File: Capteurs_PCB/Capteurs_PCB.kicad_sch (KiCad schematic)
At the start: 22 parts, among them J101 Conn_01x03, J102 Conn_01x02, J103 Conn_02x20_Odd_Even, J104 Conn_ST_STDC14, J3 Prop1, J4 Prop2, J5 Alim_Prop1, J6 Alim_Prop2, J9 LED, SW101 SW_DPDT_x2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

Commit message: Modif PCB
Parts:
- removed C104, C105, C106: 100n, symbol Device:C_Small
- removed J102: Conn_01x02, symbol Connector_Generic:Conn_01x02
- removed J3: Prop1, Connector_PinHeader_2.54mm:PinHeader_1x03_P2.54mm_Vertical, symbol Connector:Conn_01x03_Pin
- removed J4: Prop2, Connector_PinHeader_2.54mm:PinHeader_1x03_P2.54mm_Vertical, symbol Connector:Conn_01x03_Pin
- removed J6: Alim_Prop2, Connector_Hirose:Hirose_DF13-02P-1.25DSA_1x02_P1.25mm_Vertical, symbol Connector:Conn_01x02_Socket
- removed J9: LED, Connector_PinHeader_2.54mm:PinHeader_1x04_P2.54mm_Vertical, symbol Connector:Conn_01x04_Pin
- removed U101: STM32L476RGTx, Package_QFP:LQFP-64_10x10mm_P0.5mm, symbol MCU_ST_STM32L4:STM32L476RGTx
- added J1: Conn_01x04, symbol Connector_Generic:Conn_01x04
- added J2: Conn_01x03, symbol Connector_Generic:Conn_01x03
- added J3: Alim_Prop1, Connector_Hirose:Hirose_DF13-02P-1.25DSA_1x02_P1.25mm_Vertical, symbol Connector:Conn_01x02_Socket
- added U1: STM32L412KBTx, Package_QFP:LQFP-32_7x7mm_P0.8mm, symbol MCU_ST_STM32L4:STM32L412KBTx
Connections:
- net +5V: now also J101.2 (Pin_2), J2.2 (Pin_2), U1.1 (VDD), U1.17 (VDD), U1.5 (VDDA)
- net Earth: no longer J101.1 (Pin_1), J5.2 (Pin_2)
- net FWD1: now also U1.8 (PA2)
- net FWD2: now also U1.18 (PA8)
- net GND: now also J101.1 (Pin_1), J5.1 (Pin_1), J1.1 (Pin_1), J1.3 (Pin_3), J2.1 (Pin_1), J3.1 (Pin_1), U1.16 (VSS), U1.32 (VSS)
- net INT1: now also U1.6 (PA0)
- net INT2: now also U1.7 (PA1)
- net MISO: now also U1.12 (PA6)
- net MOSI: now also U1.13 (PA7)
- net REV1: now also U1.9 (PA3)
- net REV2: now also U1.19 (PA9)
- net SCLK: now also U1.11 (PA5)
- net SS: now also U1.10 (PA4)
- net SigProp1: now also J101.3 (Pin_3), J2.3 (Pin_3), U1.27 (PB4)
- net SigProp2: now also U1.29 (PB6)
- net Sig_LED: now also J1.4 (Pin_4), U1.20 (PA10)
- net UART_RX: now also U1.22 (PA12)
- net UART_TX: now also U1.21 (PA11)
- net VDD_LED: now also J1.2 (Pin_2)
- net V_ALIM_PROP: now also J5.2 (Pin_2), J3.2 (Pin_2); no longer J5.1 (Pin_1)
- no-connect marks 64 -> 38
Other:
- sheet Capteur de Pression ports: added MISO, MOSI, SCLK, SS, VDD; removed none
- sheet Gyroscope-Accéléromètre ports: added CS, IMU_MISO, IMU_MOSI, INT1, INT2, VDD, VDDIO; removed none
- note added: "RaspberryPi"
- note removed: "Branchement RaspberryPi"
- moved on the sheet: C101, C102, C103, C107, H101, H102, H103, H104, J101, J103, J104, J5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

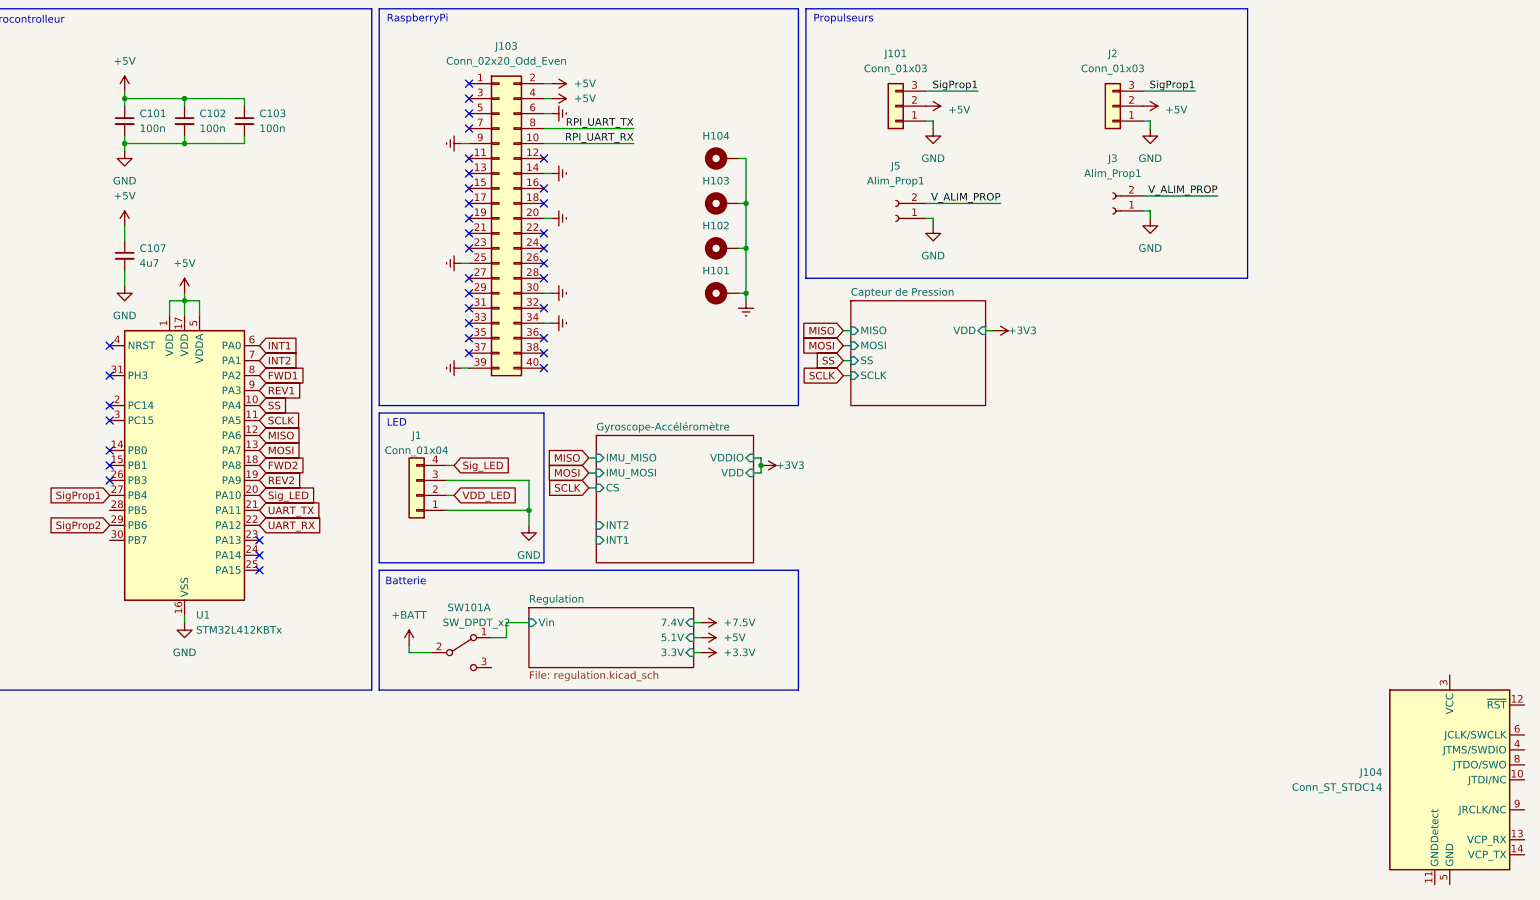
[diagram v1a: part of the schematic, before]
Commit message: kicad changes and starting footprints
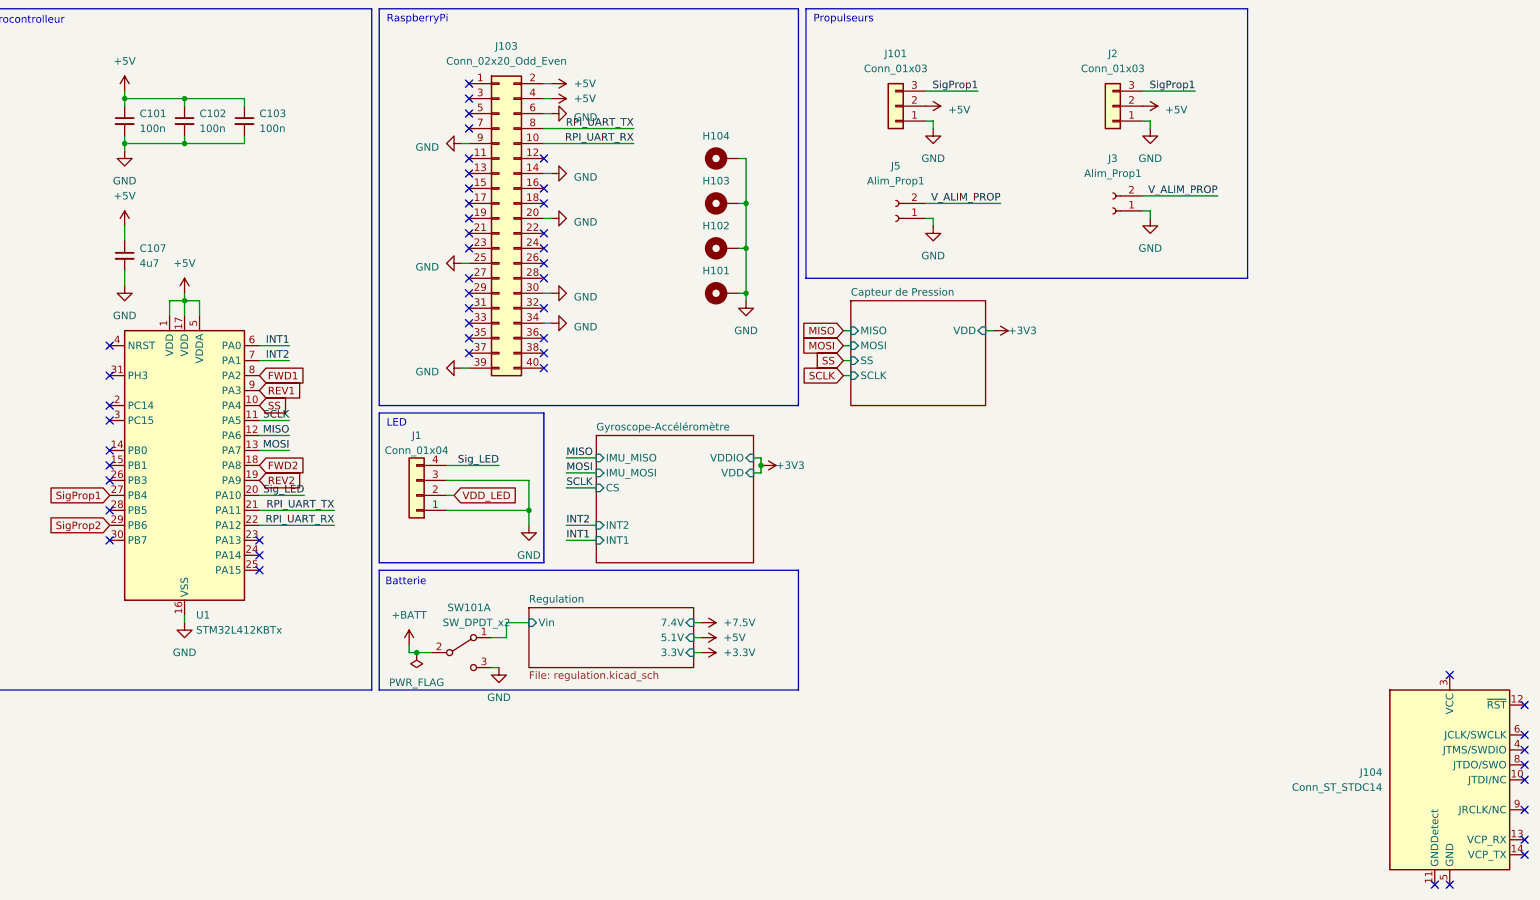
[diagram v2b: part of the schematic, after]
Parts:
- C101, C102, C103, C107: footprint (none) -> Capacitor_SMD:C_1206_3216Metric
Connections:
- net Earth is gone; now on net GND: H101.1, H102.1, H103.1, H104.1, J103.14 (Pin_14), J103.20 (Pin_20), J103.25 (Pin_25), J103.30 (Pin_30), J103.34 (Pin_34), J103.39 (Pin_39), J103.6 (Pin_6), J103.9 (Pin_9)
- net UART_RX is gone; now on net RPI_UART_RX: U1.22 (PA12)
- net UART_TX is gone; now on net RPI_UART_TX: U1.21 (PA11)
- net GND: now also SW101.3 (C)
- no-connect marks 38 -> 51

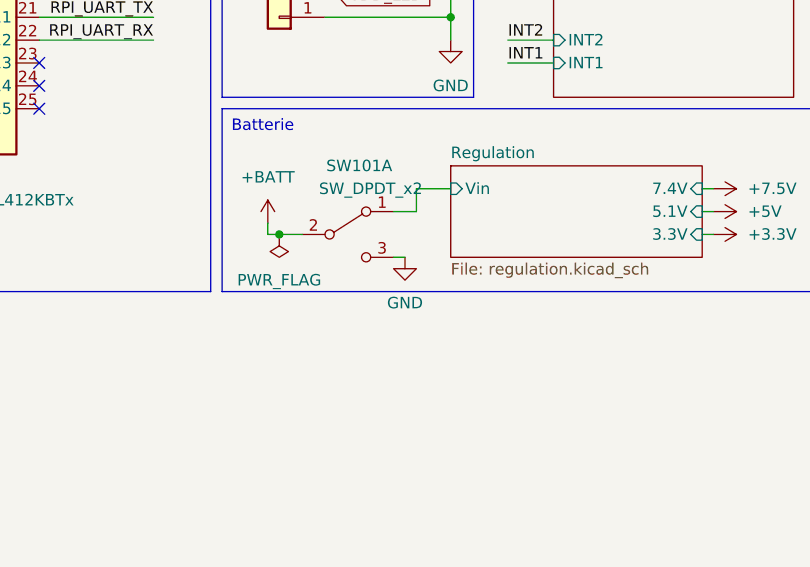
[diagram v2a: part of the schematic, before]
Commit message: Changement interrupteur
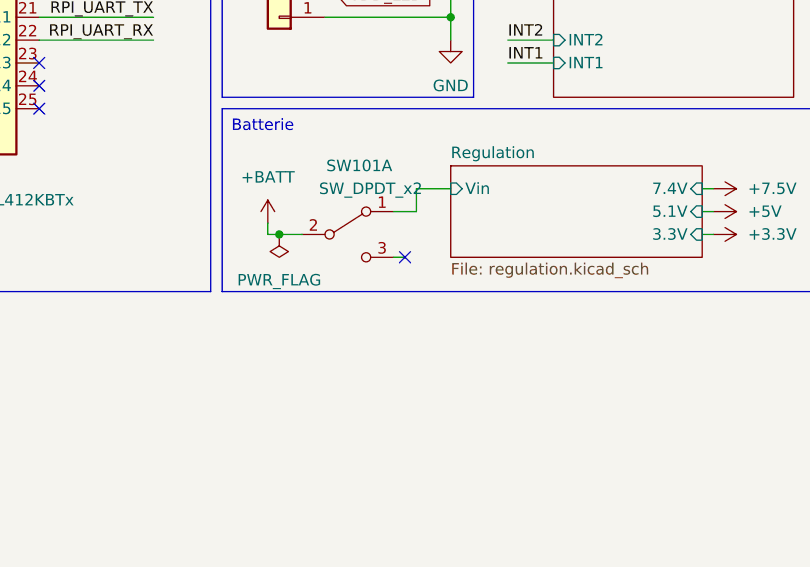
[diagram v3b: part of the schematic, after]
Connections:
- net GND: no longer SW101.3 (C)
- no-connect marks 51 -> 52
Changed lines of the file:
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@@
   (no_connect (at 97.79 29.21))
   (no_connect (at 36.83 88.9))
+  (no_connect (at 102.87 125.73))
   (no_connect (at 97.79 31.75))
   (no_connect (at 97.79 67.31))
@@
         )
       )
-    )
-  )
-  (symbol (lib_id "power:GND") (at 102.87 125.73 0) (unit 1)
-    (in_bom yes) (on_board yes) (dnp no) (fields_autoplaced)
-    (property "Reference" "#PWR017" (at 102.87 132.08 0)
-      (effects (font (size 1.27 1.27)) hide)
-    )
-    (property "Value" "GND" (at 102.87 130.81 0)
-      (effects (font (size 1.27 1.27)))
-    )
-    (property "Footprint" "" (at 102.87 125.73 0)
-      (effects (font (size 1.27 1.27)) hide)
-    )
-    (property "Datasheet" "" (at 102.87 125.73 0)
-      (effects (font (size 1.27 1.27)) hide)
-    )
-    (pin "1")
-    (instances
-      (project "Capteurs_PCB"
-        (path "/1101af8f-9425-4102-9245-339dc54562bf"
-          (reference "#PWR017") (unit 1)
-        )
-      )

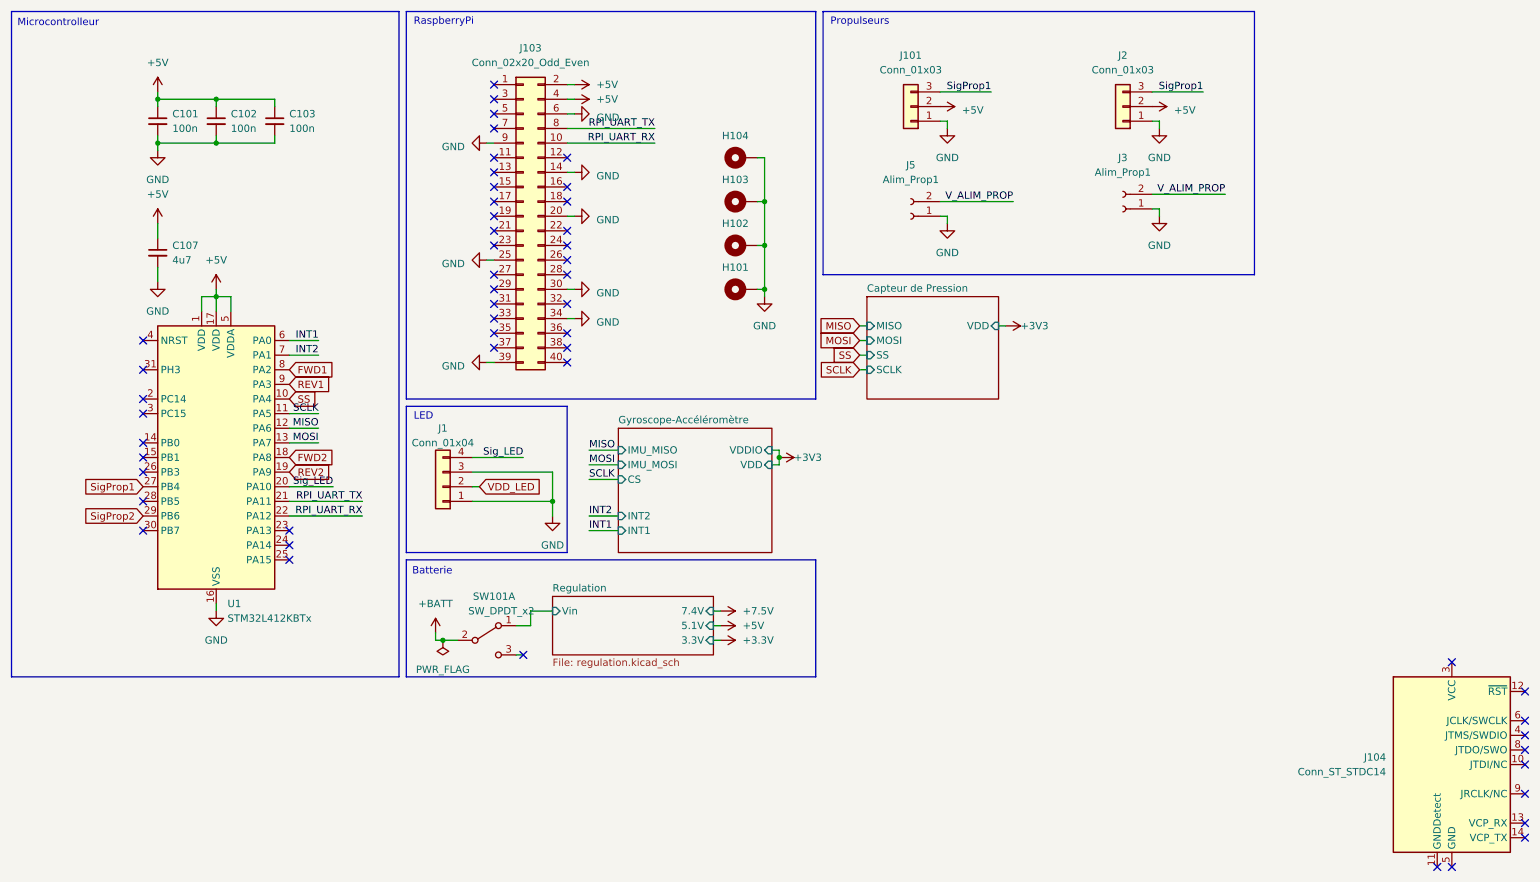
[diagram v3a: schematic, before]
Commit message: ST-LINK sur Kicad
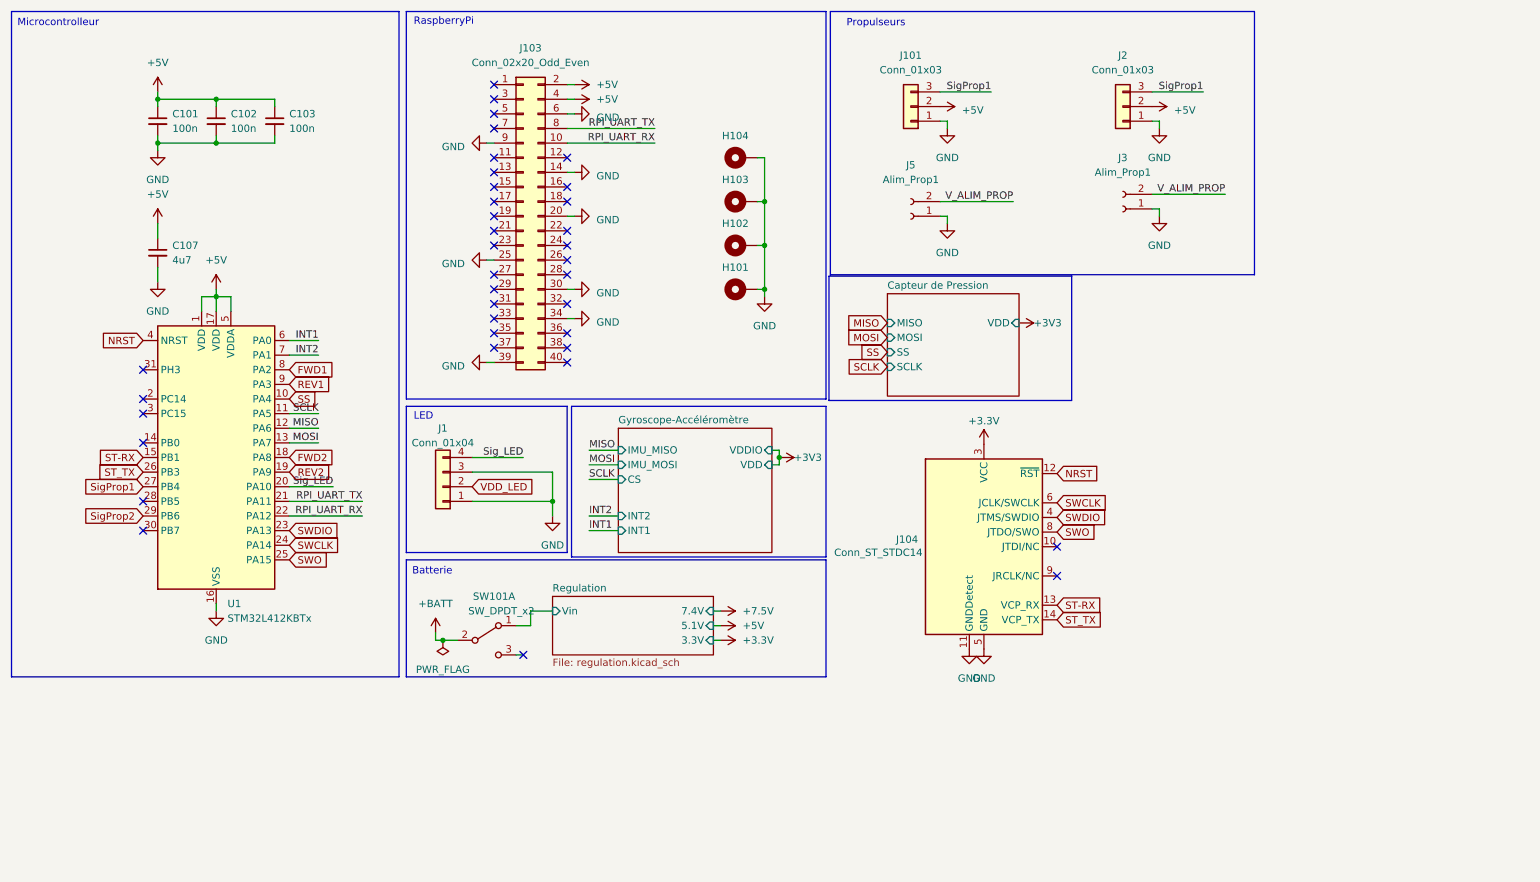
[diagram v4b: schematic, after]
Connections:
- net +3.3V: now also J104.3 (VCC)
- net GND: now also J104.11 (GNDDetect), J104.5 (GND), J104.7 (GND)
- net NRST: now reaches J104.12 (~{RST})
- net NRST: now also U1.4 (NRST)
- net ST-RX: now reaches J104.13 (VCP_RX)
- net ST-RX: now also U1.15 (PB1)
- net ST_TX: now reaches J104.14 (VCP_TX)
- net ST_TX: now also U1.26 (PB3)
- net SWDIO: now reaches J104.4 (JTMS/SWDIO)
- net SWDIO: now also U1.23 (PA13)
- net SWCLK: now reaches J104.6 (JCLK/SWCLK)
- net SWCLK: now also U1.24 (PA14)
- net SWO: now reaches J104.8 (JTDO/SWO)
- net SWO: now also U1.25 (PA15)
- no-connect marks 52 -> 37
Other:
- moved on the sheet: J104
